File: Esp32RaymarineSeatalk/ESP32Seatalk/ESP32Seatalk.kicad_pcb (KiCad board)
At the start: 2 copper layers, 35.1 x 40.1 mm, 20 parts, among them J1 SeatalkA, J2 SeatalkB, J3 CAN, J4 CANTRX, J5 GPIO2, J6 GPIO1, J7 GND, Q1 BSS138, U1 AMS1117-3.3, U2 ESP32_C3_OLED

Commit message: ESP32Seatalk hardware: KiCad project updates
Schematic and PCB edits (uncommitted since 2026-09-28), plus project settings: the ERC
pin_to_pin check is now an error and the U3 SW / BST nets are in the Power net class.

Co-Authored-By: Claude Sonnet 5.5 <noreply@anthropic.com>
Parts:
- removed U1: AMS1117-3.3, Package_TO_SOT_SMD:SOT-223-3_TabPin2
- added C5: 100nf, Capacitor_SMD:C_0805_2012Metric_Pad1.18x1.45mm_HandSolder, F.Cu at (130.4, 57.3)
- added C6: 22uf, Capacitor_Tantalum_SMD:CP_EIA-3216-12_Kemet-S_HandSolder, F.Cu at (135.8, 63.2)
- added C7: 100pf, Capacitor_SMD:C_0805_2012Metric_Pad1.18x1.45mm_HandSolder, F.Cu at (130.4, 60.3)
- added R3: 31.6k, Resistor_SMD:R_0805_2012Metric_Pad1.20x1.40mm_HandSolder, F.Cu at (135.2, 57.2)
- added R4: 10k, Resistor_SMD:R_0805_2012Metric_Pad1.20x1.40mm_HandSolder, F.Cu at (135.2, 60.2)
- added U3: AP62200, Package_TO_SOT_SMD:SOT-563, F.Cu at (129.7, 63.5)
- C1: value 4.7u -> 10u
- C3: value 4.7u -> 22uf
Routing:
- net +3.3V: track 58.5 -> 0.00 mm
- net +12V: track 54.9 -> 0.00 mm
- net CAN_RX_LL: track 33.2 -> 0.00 mm
- net HV_SEATALK: track 31.8 -> 0.00 mm
- net CAN_TX_LL: track 24.6 -> 0.00 mm
- net GND: track 19.1 -> 0.00 mm, vias 2 -> 0
- net LV_SEATALK: track 9.62 -> 0.00 mm
- net Net-(J6-Pin_1): track 6.33 -> 0.00 mm
- net Net-(J6-Pin_2): track 6.29 -> 0.00 mm
- net CANL: track 4.82 -> 0.00 mm
- net CANH: track 4.82 -> 0.00 mm
- net Net-(J6-Pin_4): track 4.77 -> 0.00 mm
- net Net-(J6-Pin_3): track 4.77 -> 0.00 mm
- net Net-(J5-Pin_1): track 4.47 -> 0.00 mm
- net Net-(J6-Pin_5): track 4.35 -> 0.00 mm
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- removed copper zone on F.Cu, net GND

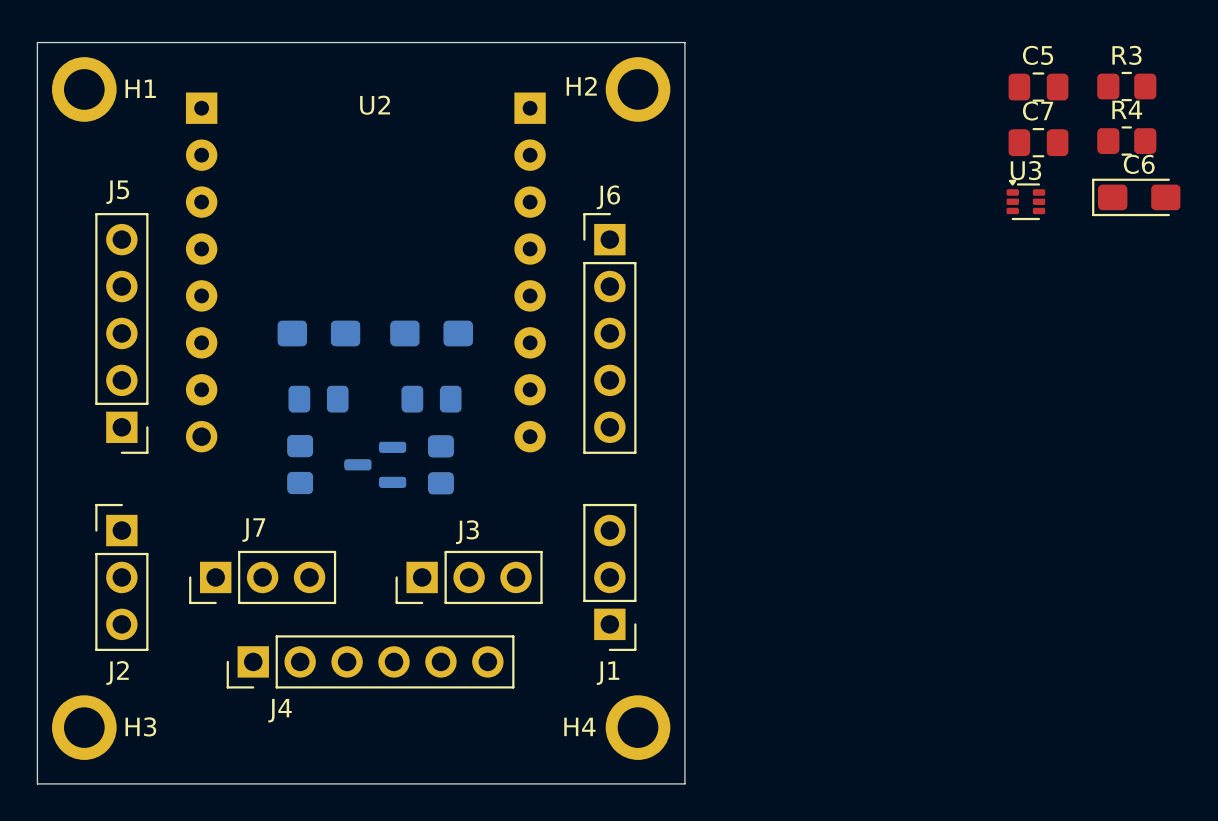
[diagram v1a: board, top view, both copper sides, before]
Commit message: Seatalk daughter board v2: AP62200 buck, 4-layer, routed, DRC clean, v2 gerbers
Schematic: AMS1117 replaced by AP62200 buck (Cyntec VCHA042A 3.3uH, 0805 ceramics),
custom L1 footprint. Board: 4 layers (In1 +3.3V, In2 GND), hand-routed, KiCad DRC with
schematic parity clean. Gerbers/drill in jlcpcb-export-v2 (v1 export untouched), design
notes and datasheets added.

Co-Authored-By: Claude Sonnet 5.5 <noreply@anthropic.com>
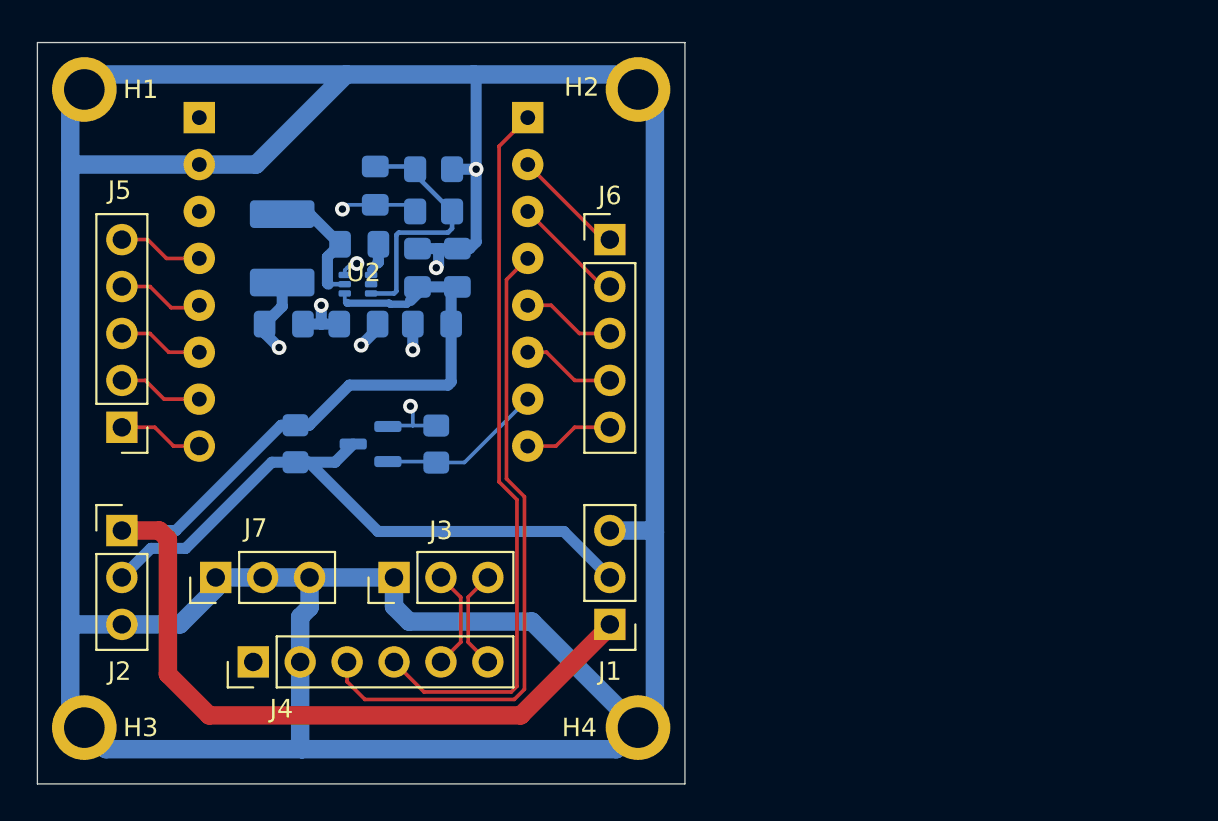
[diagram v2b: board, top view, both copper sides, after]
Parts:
- added L1: 3.3uh, Seatalk-custom:L_Cyntec_VCHA042A-MS6, B.Cu at (89.5, 66.0)
- C1: value 10u -> 22uf; footprint Capacitor_Tantalum_SMD:CP_EIA-3216-12_Kemet-S_HandSolder -> Capacitor_SMD:C_0805_2012Metric_Pad1.18x1.45mm_HandSolder
- C3: footprint Capacitor_Tantalum_SMD:CP_EIA-3216-12_Kemet-S_HandSolder -> Capacitor_SMD:C_0805_2012Metric_Pad1.18x1.45mm_HandSolder
- C4: value 100n -> 22uf
- C5, C7, R3, R4, U3: moved to B.Cu
- C6: footprint Capacitor_Tantalum_SMD:CP_EIA-3216-12_Kemet-S_HandSolder -> Capacitor_SMD:C_0805_2012Metric_Pad1.18x1.45mm_HandSolder; moved to B.Cu
- moved C6 46.8 mm to (89.5, 70.1), turned to 180 degrees
- moved R3 38.1 mm to (97.6, 64.0)
- moved C5 37.7 mm to (93.6, 65.8), turned to 180 degrees
- moved R4 37.6 mm to (97.6, 61.7)
- moved U3 36.4 mm to (93.5, 67.9)
- moved C7 36.0 mm to (94.5, 62.6), turned to 90 degrees
- moved C2 8.90 mm to (96.8, 67.1), turned to 90 degrees
- moved C4 7.25 mm to (98.9, 67.1), turned to 90 degrees
- moved C1 2.20 mm to (93.6, 70.1)
- moved J3 1.52 mm to (95.5, 83.8)
- moved Q1 1.16 mm to (94.2, 76.6)
- moved R1 1.16 mm to (97.8, 76.6)
- moved R2 1.16 mm to (90.2, 76.6)
- moved U2 0.52 mm to (93.9, 67.8)
- moved C3 0.51 mm to (97.6, 70.1), turned to 180 degrees
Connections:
- C1 pad 1: +12V -> GND
- C1 pad 2: GND -> +3.3V
- C3 pad 1: +3.3V -> +12V
- C4 pad 1: GND -> +12V
- C4 pad 2: +3.3V -> GND
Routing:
- net GND: track 0.00 -> 217.8 mm, vias 0 -> 5
- net +12V: track 0.00 -> 70.5 mm
- net CAN_RX_LL: track 0.00 -> 39.3 mm
- net CAN_TX_LL: track 0.00 -> 35.5 mm
- net HV_SEATALK: track 0.00 -> 35.1 mm
- net Net-(U3-FB): track 0.00 -> 13.9 mm
- net +3.3V: track 0.00 -> 13.7 mm, vias 0 -> 4
- net LV_SEATALK: track 0.00 -> 9.01 mm
- net Net-(U3-SW): track 0.00 -> 7.16 mm
- net Net-(J6-Pin_2): track 0.00 -> 6.13 mm
- net Net-(J6-Pin_1): track 0.00 -> 6.13 mm
- net CANH: track 0.00 -> 5.46 mm
- net CANL: track 0.00 -> 5.46 mm
- net Net-(J6-Pin_4): track 0.00 -> 5.08 mm
- net Net-(J6-Pin_3): track 0.00 -> 5.08 mm
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- added copper zone on In1.Cu, net +3.3V
- added copper zone on In2.Cu, net GND
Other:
- copper layers 2 -> 4
